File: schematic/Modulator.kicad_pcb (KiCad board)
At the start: 2 copper layers, 170 x 100 mm, 40 parts, among them J1 VIDEO IN, J2 VIDEO OUT, J3 10164359-00011LF, J4 MA05-2, J5 PJ-002B, U1 74590N, U10 TXS0108EPW, U11 TXS0108EPW, U12 TXS0108EPW, U2 IDT72125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

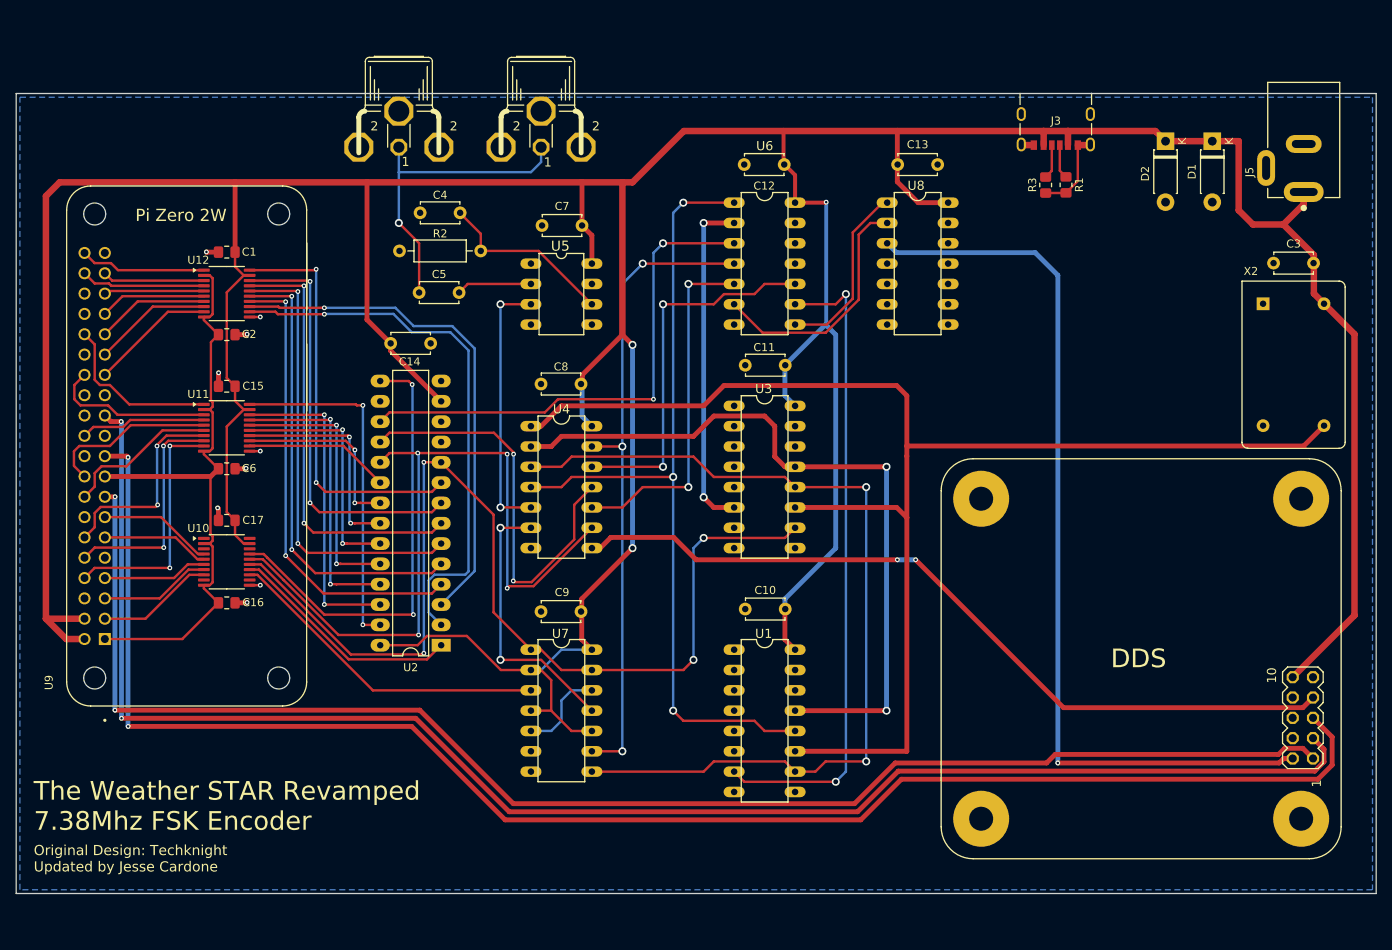
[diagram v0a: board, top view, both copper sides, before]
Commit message: Add holes for case
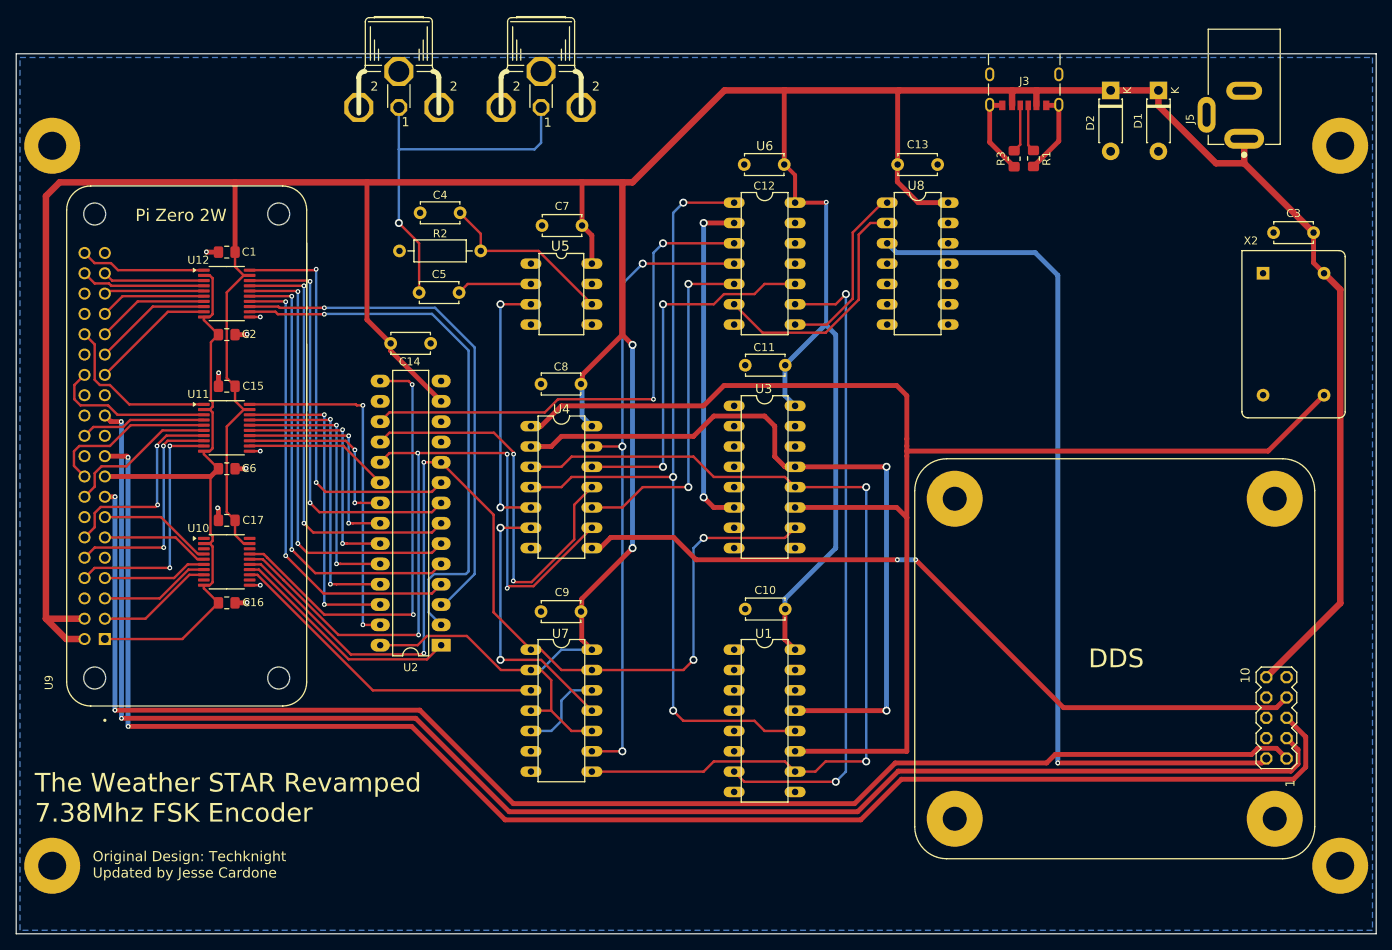
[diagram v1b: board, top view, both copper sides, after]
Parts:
- added REF**: MountingHole_3.5mm_Pad, MountingHole:MountingHole_3.5mm_Pad, F.Cu at (62.0, 61.5)
- added REF**: MountingHole_3.5mm_Pad, MountingHole:MountingHole_3.5mm_Pad, F.Cu at (223.0, 151.5)
- added REF**: MountingHole_3.5mm_Pad, MountingHole:MountingHole_3.5mm_Pad, F.Cu at (62.0, 151.5)
- added REF**: MountingHole_3.5mm_Pad, MountingHole:MountingHole_3.5mm_Pad, F.Cu at (223.0, 61.5)
- moved J5 9.98 mm to (211.0, 60.7)
- moved D2 9.35 mm to (194.3, 54.6)
- moved D1 9.25 mm to (200.3, 54.6)
- moved J3 6.34 mm to (183.5, 53.5)
- moved R1 5.24 mm to (184.7, 63.1)
- moved R3 5.13 mm to (182.2, 63.2)
- moved J1 4.97 mm to (123.1, 57.3)
- moved J2 4.97 mm to (105.3, 57.3)
- moved C3 3.81 mm to (219.7, 72.4)
- moved X2 3.81 mm to (213.4, 77.5)
- moved J4 3.30 mm to (194.8, 125.7)
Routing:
- net +5V: track 618.8 -> 629.6 mm
- net GND: track 25.6 -> 34.5 mm
- net Net-(C5-Pad2): track 39.4 -> 46.7 mm
- net /RST: track 100.0 -> 96.7 mm
- net /FSY: track 185.9 -> 182.6 mm
- net /FS: track 113.5 -> 110.2 mm
- net /SDA: track 201.7 -> 198.5 mm
- net /SCK: track 200.7 -> 197.7 mm
- net Net-(U1A-CLK): track 175.7 -> 177.6 mm
- net Net-(J3-CC2): track 4.31 -> 5.98 mm
- net Net-(J3-CC1): track 4.29 -> 5.91 mm
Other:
- board size 170 x 100 mm -> 170 x 110 mm
